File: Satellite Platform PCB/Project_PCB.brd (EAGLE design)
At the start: 115.5 x 68.2 mm, 32 parts, among them IC1 A4990KLPTR-T, IC4 A4990KLPTR-T

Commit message: Finished wiring
still need names layer
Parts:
- moved U$2 15.2 mm to (44.2, 54.5)
- moved R6 14.5 mm to (88.9, 12.7), turned to 180 degrees
- moved C3 13.7 mm to (88.8, 61.3), turned to 0 degrees
- moved R1 11.7 mm to (96.6, 59.1)
- moved R2 11.5 mm to (18.8, 17.8), turned to 90 degrees
- moved R4 10.2 mm to (10.2, 36.8), turned to 270 degrees
- moved IMU 10.2 mm to (80.0, 6.35)
- moved C6 9.67 mm to (27.7, 17.8)
- moved C7 8.92 mm to (23.4, 17.8)
- moved R3 7.80 mm to (96.0, 43.6), turned to 0 degrees
- moved R5 7.62 mm to (82.5, 12.7), turned to 180 degrees
- moved IC4 6.48 mm to (22.9, 31.8)
- moved MOTOR2 6.48 mm to (7.62, 27.9)
- moved C8 6.48 mm to (33.0, 30.5)
- moved C5 6.48 mm to (31.8, 35.6)
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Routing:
- net N$25: track 0.00 -> 171.5 mm, vias 0 -> 10
- net VCC: track 0.00 -> 164.0 mm, vias 0 -> 4
- net N$24: track 0.00 -> 76.8 mm, vias 0 -> 4
- net N$23: track 0.00 -> 71.1 mm, vias 0 -> 4
- net N$44: track 0.00 -> 68.5 mm, vias 0 -> 2
- net N$27: track 0.00 -> 65.9 mm, vias 0 -> 2
- net N$26: track 0.00 -> 65.3 mm, vias 0 -> 2
- net N$9: track 0.00 -> 52.4 mm
- net N$21: track 59.3 -> 110.3 mm, vias 0 -> 4
- net N$41: track 0.00 -> 49.9 mm
- net N$8: track 0.00 -> 45.6 mm, vias 0 -> 2
- net N$39: track 0.00 -> 37.7 mm, vias 0 -> 2
- net N$7: track 0.00 -> 36.4 mm, vias 0 -> 2
- net N$40: track 0.00 -> 35.0 mm, vias 0 -> 2
- net N$16: track 0.00 -> 33.8 mm, vias 0 -> 4
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
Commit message: Added Pin Labels
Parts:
- R1, R3, R4: value 375 mOhm -> 375 mΩ
- R2: value 375 mOhm -> 375mΩ
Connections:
- removed net N$44: R6.1, U$1.P30
- new net N$36: R6.1, U$1.P36
- net N$5: now also GPS1.2; no longer GPS1.4
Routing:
- net N$44: track 68.5 -> 0.00 mm, vias 2 -> 0
- net N$36: track 0.00 -> 54.3 mm
- net N$5: track 26.4 -> 31.5 mm
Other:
- board text added: "(+)"
- board text added: "(-)"
- board text added: "2S Battery"
- board text added: "3S Battery"
- board text added: "EN"
- board text added: "GND"
- board text added: "Motor 1"
- board text added: "Out 1"
- board text added: "Out 2"
- board text added: "Out 3"
- board text added: "Out 4"
- board text added: "SCL"
- board text added: "SDA"
- board text added: "USB"
- board text added: "Vcc"

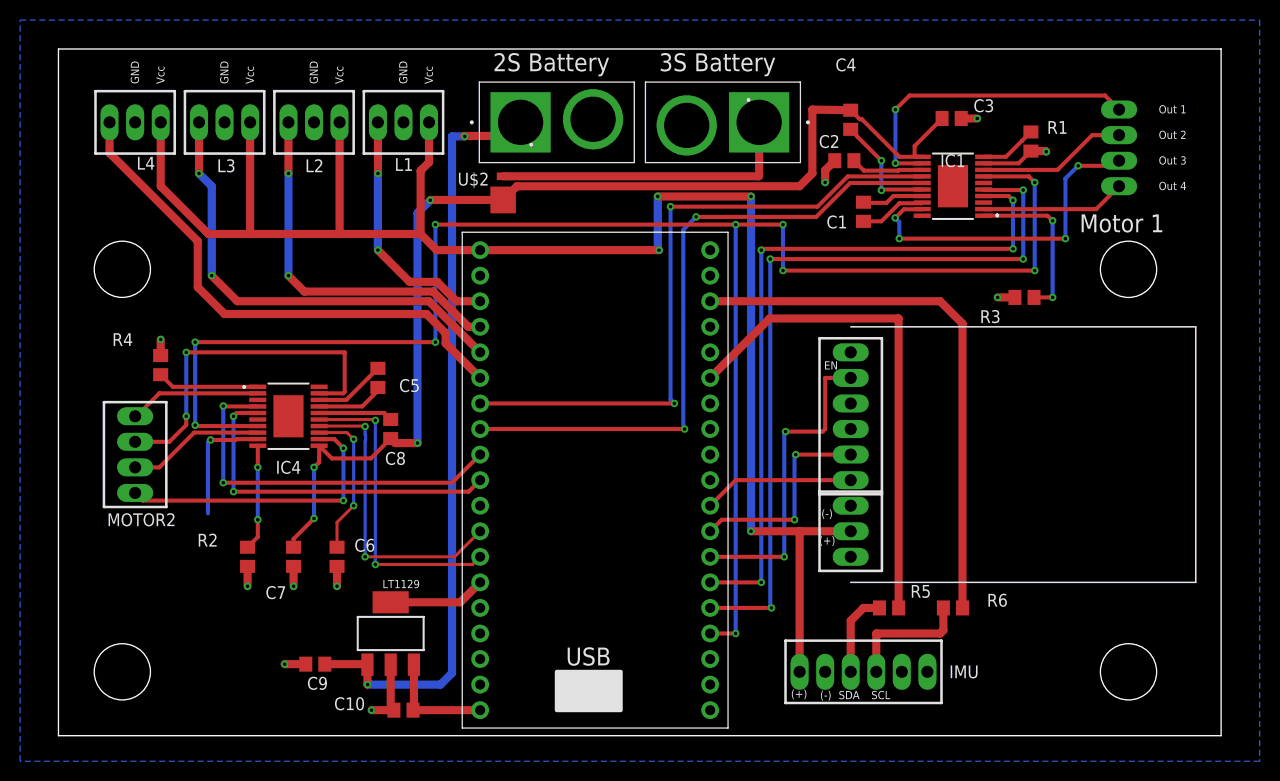
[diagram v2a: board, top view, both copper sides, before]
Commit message: Fixed names
moved all names to tnames layer, noted orientation of motor driver chips, organized labels
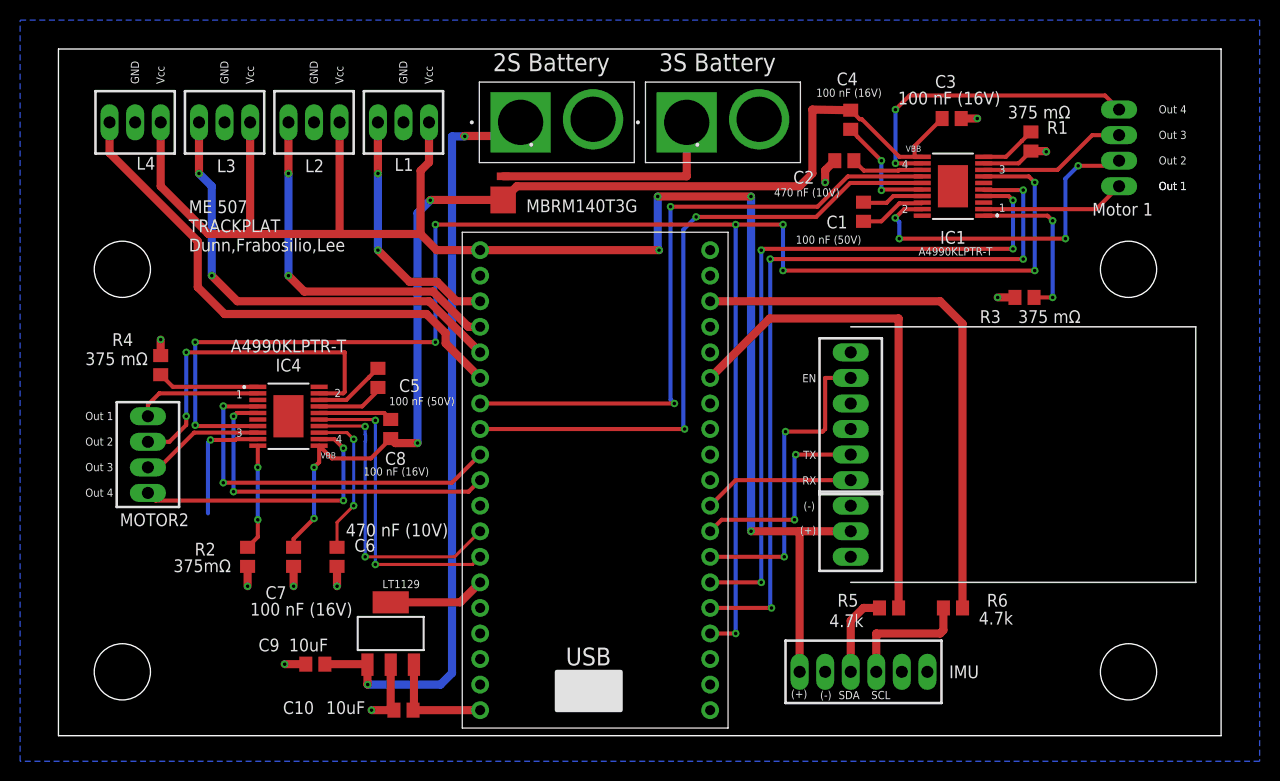
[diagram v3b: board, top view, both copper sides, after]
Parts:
- moved MOTOR2 1.27 mm to (8.89, 27.9)
- turned 3S_BATTERY to 0 degrees
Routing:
- net N$3: track 30.8 -> 23.6 mm
- net N$33: track 13.6 -> 12.4 mm
- net N$32: track 35.3 -> 34.0 mm
- net N$30: track 29.0 -> 27.7 mm
- net N$31: track 13.1 -> 12.5 mm
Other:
- board text added: "1"
- board text added: "2"
- board text added: "3"
- board text added: "4"
- board text added: "ME 507 TRACKPLAT Dunn,Frabosilio,Lee"
- board text added: "RX"
- board text added: "TX"
- board text added: "VBB"
